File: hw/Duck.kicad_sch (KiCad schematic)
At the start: 40 parts, among them J1 Conn_01x06, J2 Conn_01x04, J3 USB_C_Receptacle_USB2.0_14P, J4 Conn_01x06, Q1 MMBT3904, Q2 MMBT3904, U1 ESP32-S3-PICO-1, U2 PY32F003F1xU6, U3 SPX3819M5-L-3-3, U4 INMP441, U5 MAX17048G+T10, U6 CH343P, Y1 24.576MHz 12pF

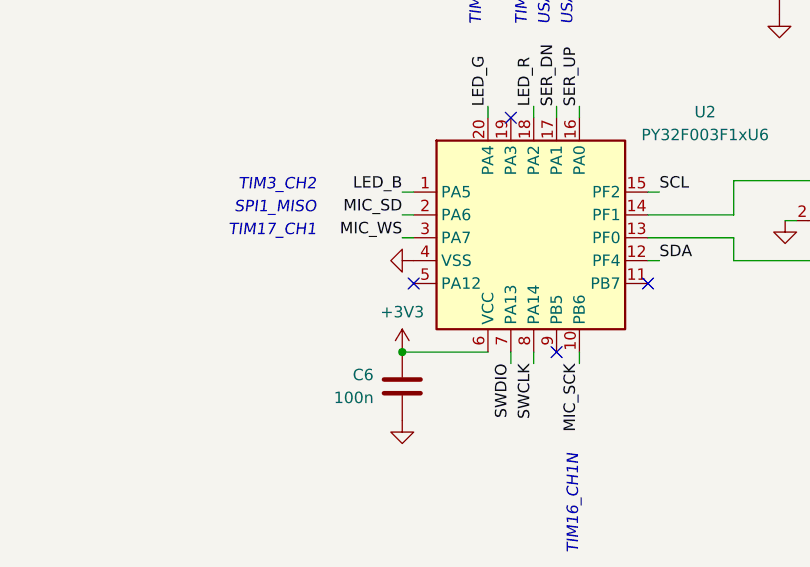
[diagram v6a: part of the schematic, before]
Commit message: hw: 🚧 Do we give up this small form factor?
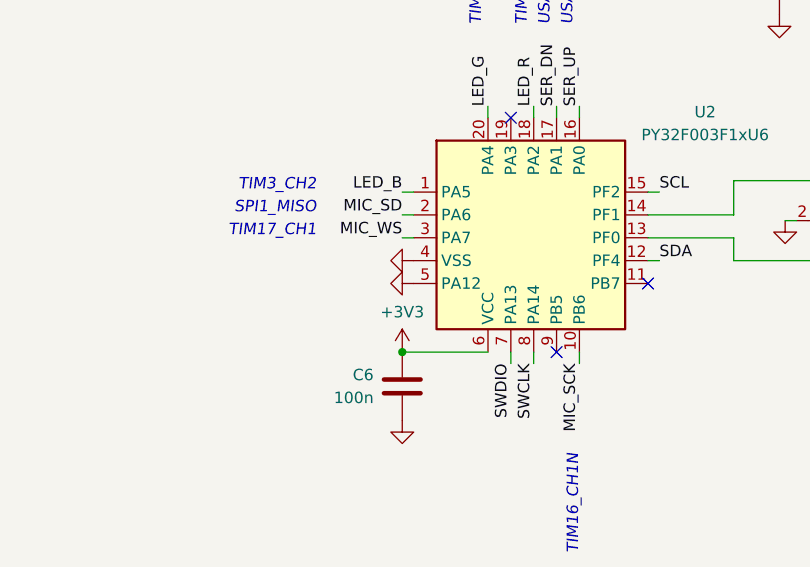
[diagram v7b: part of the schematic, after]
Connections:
- net GND: now also U2.5 (PA12)
- no-connect marks 46 -> 45
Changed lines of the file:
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@@
   (no_connect (at 128.27 60.96))
   (no_connect (at 226.06 138.43))
-  (no_connect (at 65.405 116.205))
   (no_connect (at 168.91 38.1))
   (no_connect (at 186.69 50.8))
@@
         )
       )
+    )
+  )
+  (symbol (lib_id "power:GND") (at 65.405 116.205 270) (unit 1)
+    (in_bom yes) (on_board yes) (dnp no) (fields_autoplaced)
+    (property "Reference" "#PWR020" (at 59.055 116.205 0)
+      (effects (font (size 1.27 1.27)) hide)
+    )
+    (property "Value" "GND" (at 60.96 116.205 0)
+      (effects (font (size 1.27 1.27)) hide)
+    )
+    (property "Footprint" "" (at 65.405 116.205 0)
+      (effects (font (size 1.27 1.27)) hide)
+    )
+    (property "Datasheet" "" (at 65.405 116.205 0)
+      (effects (font (size 1.27 1.27)) hide)
+    )
+    (pin "1")
+    (instances
+      (project "Duck"
+        (path "/23349607-acbb-4aa4-80bb-d6050790beec"
+          (reference "#PWR020") (unit 1)
+        )
+      )

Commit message: hw: Further simplify 🚧
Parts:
- removed C6: 100n, Capacitor_SMD:C_0402_1005Metric, symbol Device:C
- removed C7, C8: 6.8p, Capacitor_SMD:C_0402_1005Metric, symbol Device:C
- removed J2: Conn_01x04, Duck_footprints:TestPoints_1x04_P2.0, symbol Connector_Generic:Conn_01x04
- removed U2: PY32F003F1xU6, Package_DFN_QFN:QFN-20-1EP_3x3mm_P0.4mm_EP1.65x1.65mm, symbol PY32F003:PY32F003F1xU6
- removed Y1: 24.576MHz 12pF, Crystal:Crystal_SMD_2016-4Pin_2.0x1.6mm, symbol Device:Crystal_GND24
- added R2, R3: 4.7k, Resistor_SMD:R_0402_1005Metric, symbol Device:R
- renumbered C15 to C10, C9 to C4, C10 to C5, C11 to C6, C12 to C7, C13 to C8, C14 to C9, J4 to J2, U3 to U2, U4 to U3, U5 to U4, U6 to U5
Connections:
- net SER_UP is gone; now on net LED_B: U1.36 (GPIO48/SPICLK_N)
- net +3V3: now also R2.1, R3.1
- net LED_G: now also U1.38 (GPIO33)
- net LED_R: now also U1.37 (GPIO47/SPICLK_P)
- net MIC_SCK: now also U1.6 (GPIO1), U1.7 (GPIO2)
- net MIC_SD: now also U1.8 (GPIO3)
- net MIC_WS: now also U1.9 (GPIO4)
- net SCL: now also U1.26 (USB_D+/GPIO20), R2.2
- net SDA: now also U1.25 (USB_D-/GPIO19), R3.2
- net SER_DN: no longer names the net of U1.27 (GPIO21)
- no-connect marks 45 -> 35
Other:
- note removed: "SPI1_MISO"
- note removed: "TIM16_CH1N"
- note removed: "TIM17_CH1"
- note removed: "TIM3_CH1"
- note removed: "TIM3_CH2"
- note removed: "TIM3_CH3"
- note removed: "USART2_RX"
- note removed: "USART2_TX"
- moved on the sheet: C6, C7, U3, U4
